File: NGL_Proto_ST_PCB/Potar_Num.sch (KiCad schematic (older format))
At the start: 2 parts, among them U10 10K, U11 AD5270BRMZ-20-RL7

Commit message: amélioration
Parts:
- added C30: C, Capacitor_SMD:C_0805_2012Metric, symbol Device:C
- U11: value AD5270BRMZ-20-RL7 -> 20k; OC_FARNELL - -> (none); PACKAGE MSOP-10 -> (none)
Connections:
- net +3V3: now also U10.1 (VDD), U10.6 (SPI/*UD), U11.1 (VDD)
- net GND: now also U10.14 (VSS), U10.2 (GND), U11.4 (VSS), U11.6 (GND), C30.2
- net R2_OUT: now reaches U10.10 (L)
- net R2_IN: now reaches U10.12 (H)
- net CS_R2: now reaches U10.3 (*CS)
- net CLK: now reaches U10.4 (SCLK_*INC)
- net CLK: now also U11.9 (SCLK)
- net MOSI: now reaches U10.5 (DIN_U/*D)
- net MOSI: now also U11.8 (DIN)
- net CS_R10: now reaches U11.10 (~SYNC)
- net R10_IN: now reaches U11.2 (A)
- net R10_OUT: now reaches U11.3 (W)
- net at U11.5 (EXT_CAP): now also C30.1
- no-connect marks 0 -> 5
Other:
- note added: "1 pour SPI"
- note added: "Entrée RES"
- note added: "Voir montage"
- moved on the sheet: U11
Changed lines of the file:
@@
 $EndDescr
+$Comp
+L power:+3.3V #PWR015
+U 1 1 62947A80
+P 6665 3645
+F 0 "#PWR015" H 6665 3495 50  0001 C CNN
+F 1 "+3.3V" H 6680 3818 50  0000 C CNN
+F 2 "" H 6665 3645 50  0001 C CNN
+F 3 "" H 6665 3645 50  0001 C CNN
+	1    6665 3645
+	1    0    0    -1
+$EndComp
+$Comp
+L power:GND #PWR016
+U 1 1 629496F5
+P 5375 4050
+F 0 "#PWR016" H 5375 3800 50  0001 C CNN
+F 1 "GND" H 5380 3877 50  0000 C CNN
+F 2 "" H 5375 4050 50  0001 C CNN
+F 3 "" H 5375 4050 50  0001 C CNN
+	1    5375 4050
+	0    -1   -1   0
+$EndComp
+Text Notes 3720 1810 0    197  Italic 39
+POTENTIOMÈTRE NUMÉRIQUE
+Text Notes 9825 4720 0    50   ~ 0
+10 Bits 1024 Positions\nAlimentation en 3.3V
+$Comp
+L AD5270BRMZ-20-RL7:AD5270BRMZ-20-RL7 U11
+U 1 1 6295B510
+P 7565 4425
+F 0 "U11" H 7560 5205 50  0000 C CNN
+F 1 "20k" H 7565 5004 50  0000 C CNN
+F 2 "Lib_NGL_ST:SOP50P490X110-10N" H 7565 4425 50  0001 L BNN
+F 3 "https://www.analog.com/media/en/technical-documentation/data-sheets/AD5270_5271.pdf" H 7565 4425 50  0001 L BNN
+F 4 "Analog Devices" H 7565 4425 50  0001 L BNN "SUPPLIER"
+F 5 "52R8111" H 7565 4425 50  0001 L BNN "OC_NEWARK"
+F 6 "AD5270BRMZ-20-RL7" H 7145 5080 50  0000 L BNN "MPN"
+	1    7565 4425
+	1    0    0    -1
+$EndComp
+Text GLabel 4975 5100 2    50   BiDi ~ 0
+CLK
+Text GLabel 4980 5300 2    50   BiDi ~ 0
+CS_R2
+Text GLabel 6680 4425 0    50   Input ~ 0
+MOSI
+Text Notes 5260 5230 0    50   ~ 0
+Entrée RES
+Text GLabel 4890 4800 2    50   BiDi ~ 0
+R2_IN
+Text GLabel 4890 4700 2    50   Output ~ 0
+R2_OUT
+Text GLabel 8485 4125 2    50   BiDi ~ 0
+R10_IN
+Text GLabel 8495 4225 2    50   Output ~ 0
+R10_OUT
+Text GLabel 6685 4525 0    50   BiDi ~ 0
+CLK
+$Comp
+L power:GND #PWR042
+U 1 1 629B014D
+P 6670 5230
+F 0 "#PWR042" H 6670 4980 50  0001 C CNN
+F 1 "GND" H 6675 5057 50  0000 C CNN
+F 2 "" H 6670 5230 50  0001 C CNN
+F 3 "" H 6670 5230 50  0001 C CNN
+	1    6670 5230
+	1    0    0    -1
+$EndComp
+Text GLabel 4980 5200 2    50   Input ~ 0
+MOSI
+NoConn ~ 8265 4425
+Wire Wire Line
+	4980 5200 4710 5200
+Wire Wire Line
+	4710 5100 4975 5100
+Wire Wire Line
+	4890 4800 4710 4800
+Wire Wire Line
+	4890 4700 4710 4700
+Text Notes 4435 4460 0    50   ~ 0
+Voir montage
+$Comp
+L power:+3.3V #PWR040
+U 1 1 629B80B0
+P 4995 3645
+F 0 "#PWR040" H 4995 3495 50  0001 C CNN
+F 1 "+3.3V" H 5010 3818 50  0000 C CNN
+F 2 "" H 4995 3645 50  0001 C CNN
+F 3 "" H 4995 3645 50  0001 C CNN
+	1    4995 3645
+	1    0    0    -1
+$EndComp
+Wire Wire Line
+	4710 4000 4890 4000
+Wire Wire Line
+	4890 4000 4890 4050
+Wire Wire Line
+	4890 4050 5375 4050
+Wire Wire Line
+	4710 4100 4890 4100
+Wire Wire Line
+	4890 4100 4890 4050
+Connection ~ 4890 4050
+Wire Wire Line
+	4995 3645 4995 4300
+Wire Wire Line
+	4995 4300 4710 4300
+Wire Wire Line
+	6665 3645 6665 4125
+Wire Wire Line
+	6665 4125 6865 4125
+Wire Wire Line
+	8485 4125 8265 4125
+Wire Wire Line
+	8495 4225 8265 4225
+Wire Wire Line
+	6865 4425 6680 4425
+Wire Wire Line
+	6865 4525 6685 4525
+Wire Wire Line
+	6670 5025 6865 5025
+Wire Wire Line
+	6865 4825 6670 4825
+Wire Wire Line
+	6670 4825 6670 5025
+Connection ~ 6670 5025
+Wire Wire Line
+	6670 5025 6670 5230
+NoConn ~ 2910 5000
+NoConn ~ 2910 4900
+NoConn ~ 2910 4800
+NoConn ~ 2910 4700
 $Comp
 L max5481eud&plus_T:max5481eud+T U10
@@
 	-1   0    0    1
 $EndComp
+Text GLabel 6685 4625 0    50   Input ~ 0
+CS_R10
+Wire Wire Line
+	6865 4625 6685 4625
 $Comp
-L power:+3.3V #PWR015
-U 1 1 62947A80
-P 3550 3620
-F 0 "#PWR015" H 3550 3470 50  0001 C CNN
-F 1 "+3.3V" H 3565 3793 50  0000 C CNN
-F 2 "" H 3550 3620 50  0001 C CNN
-F 3 "" H 3550 3620 50  0001 C CNN
-	1    3550 3620
+L Device:C C30
+U 1 1 629BEC75
+P 6085 4510
+F 0 "C30" H 6200 4556 50  0000 L CNN
+F 1 "C" H 6200 4465 50  0000 L CNN
+F 2 "Capacitor_SMD:C_0805_2012Metric" H 6123 4360 50  0001 C CNN
+F 3 "~" H 6085 4510 50  0001 C CNN
+	1    6085 4510
 	1    0    0    -1
 $EndComp
-$Comp
-L power:GND #PWR016
-U 1 1 629496F5
-P 3820 6170
-F 0 "#PWR016" H 3820 5920 50  0001 C CNN
-F 1 "GND" H 3825 5997 50  0000 C CNN
-F 2 "" H 3820 6170 50  0001 C CNN
-F 3 "" H 3820 6170 50  0001 C CNN
-	1    3820 6170
-	1    0    0    -1
-$EndComp
-Text Notes 3720 1810 0    197  Italic 39
-POTENTIOMÈTRE NUMÉRIQUE
-Text Notes 7820 4660 0    50   ~ 0
-10 Bits 1024 Positions\nAlimentation en 3.3V
-$Comp
-L AD5270BRMZ-20-RL7:AD5270BRMZ-20-RL7 U11
-U 1 1 6295B510
-P 6220 4500
-F 0 "U11" H 6220 5170 50  0000 C CNN
-F 1 "AD5270BRMZ-20-RL7" H 6220 5079 50  0000 C CNN
-F 2 "Lib_NGL_ST:SOP50P490X110-10N" H 6220 4500 50  0001 L BNN
-F 3 "https://www.analog.com/media/en/technical-documentation/data-sheets/AD5270_5271.pdf" H 6220 4500 50  0001 L BNN
-F 4 "Analog Devices" H 6220 4500 50  0001 L BNN "SUPPLIER"
-F 5 "52R8111" H 6220 4500 50  0001 L BNN "OC_NEWARK"
-F 6 "MSOP-10" H 6220 4500 50  0001 L BNN "PACKAGE"
-F 7 "AD5270BRMZ-20-RL7" H 6220 4500 50  0001 L BNN "MPN"
-F 8 "-" H 6220 4500 50  0001 L BNN "OC_FARNELL"
-	1    6220 4500
-	1    0    0    -1
-$EndComp
+Wire Wire Line
+	6865 4325 6085 4325
+Wire Wire Line
+	6085 4325 6085 4360
+Wire Wire Line
+	6085 4660 6085 4825
+Wire Wire Line
+	6085 4825 6670 4825
+Connection ~ 6670 4825
+Wire Wire Line
+	4980 5300 4710 5300
+Wire Wire Line
+	4995 4300 4995 5000
+Wire Wire Line
+	4995 5000 4710 5000
+Connection ~ 4995 4300
+Text Notes 5080 5000 0    50   ~ 0
+1 pour SPI
 $EndSCHEMATC

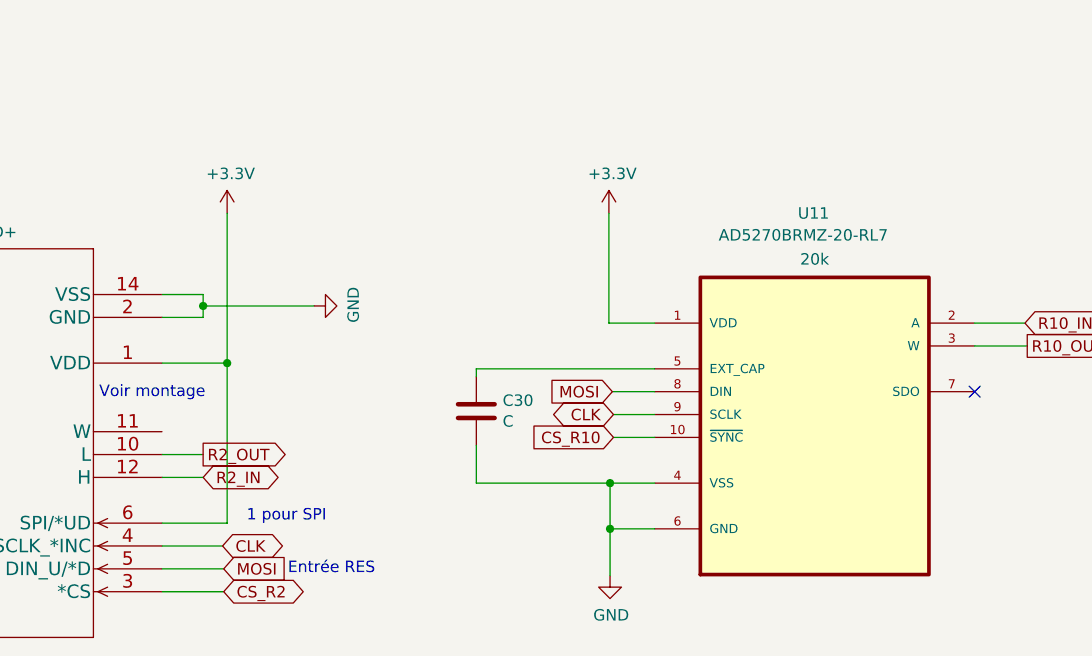
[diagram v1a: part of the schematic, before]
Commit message: Ajuut nouveaux composants: commande 3
Attente question ENABL E + POTAR
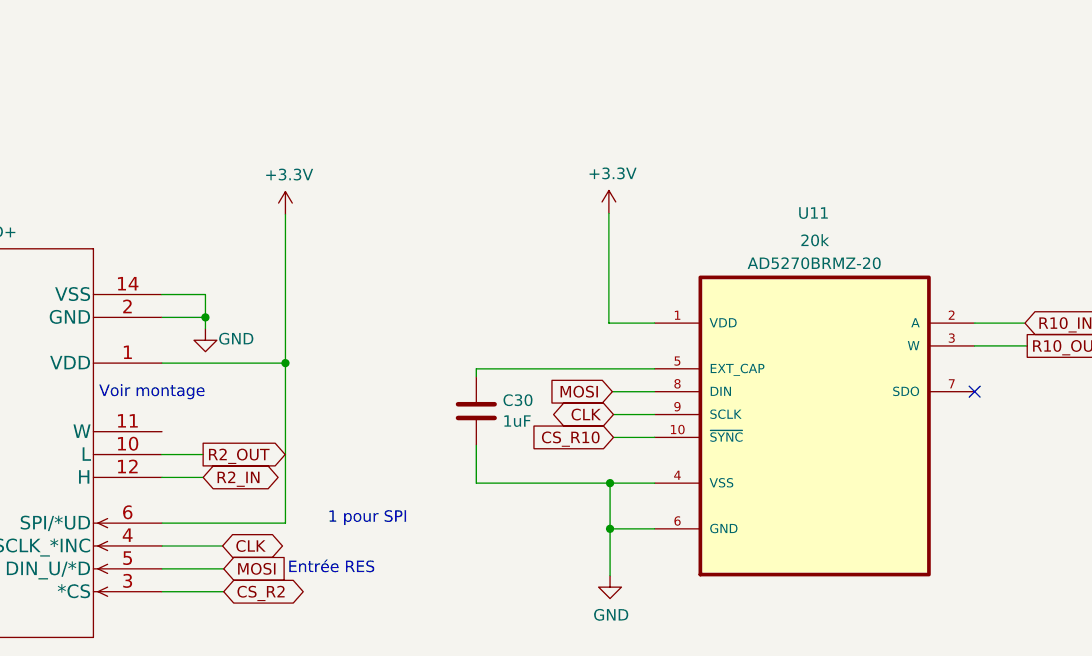
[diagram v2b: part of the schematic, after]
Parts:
- C30: value C -> 1uF
- U11: MPN AD5270BRMZ-20-RL7 -> AD5270BRMZ-20
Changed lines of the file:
@@
 L power:GND #PWR016
 U 1 1 629496F5
-P 5375 4050
-F 0 "#PWR016" H 5375 3800 50  0001 C CNN
-F 1 "GND" H 5380 3877 50  0000 C CNN
-F 2 "" H 5375 4050 50  0001 C CNN
-F 3 "" H 5375 4050 50  0001 C CNN
-	1    5375 4050
-	0    -1   -1   0
+P 4900 4150
+F 0 "#PWR016" H 4900 3900 50  0001 C CNN
+F 1 "GND" H 5035 4105 50  0000 C CNN
+F 2 "" H 4900 4150 50  0001 C CNN
+F 3 "" H 4900 4150 50  0001 C CNN
+	1    4900 4150
+	1    0    0    -1
 $EndComp
 Text Notes 3720 1810 0    197  Italic 39
@@
 P 7565 4425
 F 0 "U11" H 7560 5205 50  0000 C CNN
-F 1 "20k" H 7565 5004 50  0000 C CNN
+F 1 "20k" H 7565 5085 50  0000 C CNN
 F 2 "Lib_NGL_ST:SOP50P490X110-10N" H 7565 4425 50  0001 L BNN
 F 3 "https://www.analog.com/media/en/technical-documentation/data-sheets/AD5270_5271.pdf" H 7565 4425 50  0001 L BNN
 F 4 "Analog Devices" H 7565 4425 50  0001 L BNN "SUPPLIER"
 F 5 "52R8111" H 7565 4425 50  0001 L BNN "OC_NEWARK"
-F 6 "AD5270BRMZ-20-RL7" H 7145 5080 50  0000 L BNN "MPN"
+F 6 "AD5270BRMZ-20" H 7565 4985 50  0000 C CNN "MPN"
 	1    7565 4425
 	1    0    0    -1
@@
 L power:+3.3V #PWR040
 U 1 1 629B80B0
-P 4995 3645
-F 0 "#PWR040" H 4995 3495 50  0001 C CNN
-F 1 "+3.3V" H 5010 3818 50  0000 C CNN
-F 2 "" H 4995 3645 50  0001 C CNN
-F 3 "" H 4995 3645 50  0001 C CNN
-	1    4995 3645
+P 5250 3650
+F 0 "#PWR040" H 5250 3500 50  0001 C CNN
+F 1 "+3.3V" H 5265 3823 50  0000 C CNN
+F 2 "" H 5250 3650 50  0001 C CNN
+F 3 "" H 5250 3650 50  0001 C CNN
+	1    5250 3650
 	1    0    0    -1
 $EndComp
-Wire Wire Line
-	4710 4000 4890 4000
-Wire Wire Line
-	4890 4000 4890 4050
-Wire Wire Line
-	4890 4050 5375 4050
-Wire Wire Line
-	4710 4100 4890 4100
-Wire Wire Line
-	4890 4100 4890 4050
-Connection ~ 4890 4050
-Wire Wire Line
-	4995 3645 4995 4300
-Wire Wire Line
-	4995 4300 4710 4300
 Wire Wire Line
 	6665 3645 6665 4125
@@
 P 6085 4510
 F 0 "C30" H 6200 4556 50  0000 L CNN
-F 1 "C" H 6200 4465 50  0000 L CNN
+F 1 "1uF" H 6200 4465 50  0000 L CNN
 F 2 "Capacitor_SMD:C_0805_2012Metric" H 6123 4360 50  0001 C CNN
 F 3 "~" H 6085 4510 50  0001 C CNN
@@
 Wire Wire Line
 	4980 5300 4710 5300
+Text Notes 5435 5010 0    50   ~ 0
+1 pour SPI
 Wire Wire Line
-	4995 4300 4995 5000
+	5250 3650 5250 4300
 Wire Wire Line
-	4995 5000 4710 5000
-Connection ~ 4995 4300
-Text Notes 5080 5000 0    50   ~ 0
-1 pour SPI
+	5250 5000 4710 5000
+Wire Wire Line
+	5250 4300 4710 4300
+Connection ~ 5250 4300
+Wire Wire Line
+	5250 4300 5250 5000
+Wire Wire Line
+	4710 4100 4900 4100
+Wire Wire Line
+	4710 4000 4900 4000
+Wire Wire Line
+	4900 4000 4900 4100
+Connection ~ 4900 4100
+Wire Wire Line
+	4900 4100 4900 4150
 $EndSCHEMATC

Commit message: Avancement après réunion mercredi
finir pour mettre en review puis attente.
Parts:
- added R39: 0R, Resistor_SMD:R_0805_2012Metric, symbol Device:R
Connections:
- net R2_IN: now also U10.11 (W); no longer U10.12 (H)
- net R2_OUT: now also R39.1
- new net: R39.2, U10.12 (H)
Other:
- note removed: "Voir montage"
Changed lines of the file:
@@
 Text Notes 5260 5230 0    50   ~ 0
 Entrée RES
-Text GLabel 4890 4800 2    50   BiDi ~ 0
+Text GLabel 4890 4600 2    50   BiDi ~ 0
 R2_IN
 Text GLabel 4890 4700 2    50   Output ~ 0
@@
 Wire Wire Line
 	4710 5100 4975 5100
-Wire Wire Line
-	4890 4800 4710 4800
-Wire Wire Line
-	4890 4700 4710 4700
-Text Notes 4435 4460 0    50   ~ 0
-Voir montage
 $Comp
 L power:+3.3V #PWR040
@@
 Wire Wire Line
 	4900 4100 4900 4150
+$Comp
+L Device:R R39
+U 1 1 62A152EA
+P 4885 4905
+F 0 "R39" V 4925 5085 50  0000 C CNN
+F 1 "0R" V 4769 4905 50  0000 C CNN
+F 2 "Resistor_SMD:R_0805_2012Metric" V 4815 4905 50  0001 C CNN
+F 3 "~" H 4885 4905 50  0001 C CNN
+	1    4885 4905
+	0    1    1    0
+$EndComp
+Wire Wire Line
+	4890 4700 4800 4700
+Wire Wire Line
+	4890 4600 4710 4600
+Wire Wire Line
+	4735 4905 4735 4800
+Wire Wire Line
+	4735 4800 4710 4800
+Wire Wire Line
+	5035 4905 5070 4905
+Wire Wire Line
+	5070 4905 5070 4820
+Wire Wire Line
+	5070 4820 4800 4820
+Wire Wire Line
+	4800 4820 4800 4700
+Connection ~ 4800 4700
+Wire Wire Line
+	4800 4700 4710 4700
 $EndSCHEMATC

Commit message: Commit avant DSN
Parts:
- added C31, C32: 100nF, Capacitor_SMD:C_0805_2012Metric_Pad1.18x1.45mm_HandSolder, symbol Device:C
- C30: footprint Capacitor_SMD:C_0805_2012Metric -> Capacitor_SMD:C_0805_2012Metric_Pad1.18x1.45mm_HandSolder
- R39: footprint Resistor_SMD:R_0805_2012Metric -> Resistor_SMD:R_0805_2012Metric_Pad1.20x1.40mm_HandSolder
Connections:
- net +3V3: now also C31.1, C32.1
- net GND: now also C31.2, C32.2
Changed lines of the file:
@@
 encoding utf-8
 Sheet 5 6
-Title "NGL_Proto_V2"
-Date "2022-05-27"
-Rev "V2"
+Title "NGL_Proto_ST"
+Date "2022-06-09"
+Rev "V1.1"
 Comp "ADTP"
 Comment1 "Auteur: Benoît"
 Comment2 "Proto avec potar numérique + intégration"
-Comment3 "Sous traité chez JLCPCB"
+Comment3 "Sous traité chez EUROCIRCUIT"
 Comment4 ""
 $EndDescr
@@
 F 0 "C30" H 6200 4556 50  0000 L CNN
 F 1 "1uF" H 6200 4465 50  0000 L CNN
-F 2 "Capacitor_SMD:C_0805_2012Metric" H 6123 4360 50  0001 C CNN
+F 2 "Capacitor_SMD:C_0805_2012Metric_Pad1.18x1.45mm_HandSolder" H 6123 4360 50  0001 C CNN
 F 3 "~" H 6085 4510 50  0001 C CNN
 	1    6085 4510
@@
 F 0 "R39" V 4925 5085 50  0000 C CNN
 F 1 "0R" V 4769 4905 50  0000 C CNN
-F 2 "Resistor_SMD:R_0805_2012Metric" V 4815 4905 50  0001 C CNN
+F 2 "Resistor_SMD:R_0805_2012Metric_Pad1.20x1.40mm_HandSolder" V 4815 4905 50  0001 C CNN
 F 3 "~" H 4885 4905 50  0001 C CNN
 	1    4885 4905
@@
 Wire Wire Line
 	4800 4700 4710 4700
+$Comp
+L Device:C C31
+U 1 1 62A4A936
+P 3800 2500
+F 0 "C31" H 3915 2546 50  0000 L CNN
+F 1 "100nF" H 3915 2455 50  0000 L CNN
+F 2 "Capacitor_SMD:C_0805_2012Metric_Pad1.18x1.45mm_HandSolder" H 3838 2350 50  0001 C CNN
+F 3 "~" H 3800 2500 50  0001 C CNN
+	1    3800 2500
+	1    0    0    -1
+$EndComp
+$Comp
+L Device:C C32
+U 1 1 62A4C6AB
+P 7500 2500
+F 0 "C32" H 7615 2546 50  0000 L CNN
+F 1 "100nF" H 7615 2455 50  0000 L CNN
+F 2 "Capacitor_SMD:C_0805_2012Metric_Pad1.18x1.45mm_HandSolder" H 7538 2350 50  0001 C CNN
+F 3 "~" H 7500 2500 50  0001 C CNN
+	1    7500 2500
+	1    0    0    -1
+$EndComp
+$Comp
+L power:GND #PWR065
+U 1 1 62A4E28A
+P 7500 2750
+F 0 "#PWR065" H 7500 2500 50  0001 C CNN
+F 1 "GND" H 7505 2577 50  0000 C CNN
+F 2 "" H 7500 2750 50  0001 C CNN
+F 3 "" H 7500 2750 50  0001 C CNN
+	1    7500 2750
+	1    0    0    -1
+$EndComp
+$Comp
+L power:+3.3V #PWR064
+U 1 1 62A4ED06
+P 7500 2250
+F 0 "#PWR064" H 7500 2100 50  0001 C CNN
+F 1 "+3.3V" H 7515 2423 50  0000 C CNN
+F 2 "" H 7500 2250 50  0001 C CNN
+F 3 "" H 7500 2250 50  0001 C CNN
+	1    7500 2250
+	1    0    0    -1
+$EndComp
+$Comp
+L power:GND #PWR063
+U 1 1 62A50038
+P 3800 2750
+F 0 "#PWR063" H 3800 2500 50  0001 C CNN
+F 1 "GND" H 3805 2577 50  0000 C CNN
+F 2 "" H 3800 2750 50  0001 C CNN
+F 3 "" H 3800 2750 50  0001 C CNN
+	1    3800 2750
+	1    0    0    -1
+$EndComp
+$Comp
+L power:+3.3V #PWR029
+U 1 1 62A52392
+P 3800 2250
+F 0 "#PWR029" H 3800 2100 50  0001 C CNN
+F 1 "+3.3V" H 3815 2423 50  0000 C CNN
+F 2 "" H 3800 2250 50  0001 C CNN
+F 3 "" H 3800 2250 50  0001 C CNN
+	1    3800 2250
+	1    0    0    -1
+$EndComp
+Wire Wire Line
+	7500 2750 7500 2650
+Wire Wire Line
+	7500 2350 7500 2250
+Wire Wire Line
+	3800 2750 3800 2650
+Wire Wire Line
+	3800 2350 3800 2250
 $EndSCHEMATC
